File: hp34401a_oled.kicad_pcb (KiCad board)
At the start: 2 copper layers, 30 x 35 mm, 32 parts, among them J1 USB_B_Micro, J2 DISPLAY, J3 UART, J4 FP, J5 DISPLAYPWR, U1 STM32F103C8Tx, U2 LM1117-3.3, Y1 8M

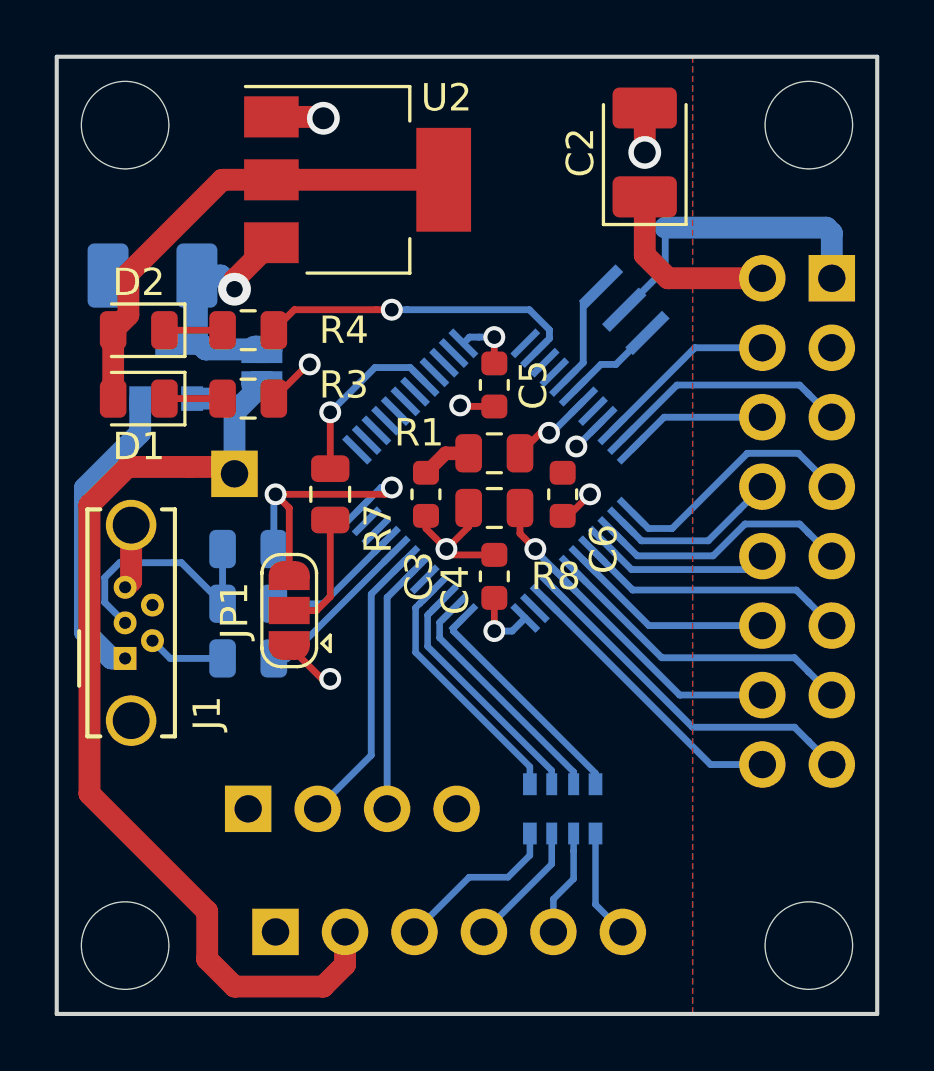
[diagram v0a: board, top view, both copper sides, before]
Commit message: Tweak size, footprints, generate gerber
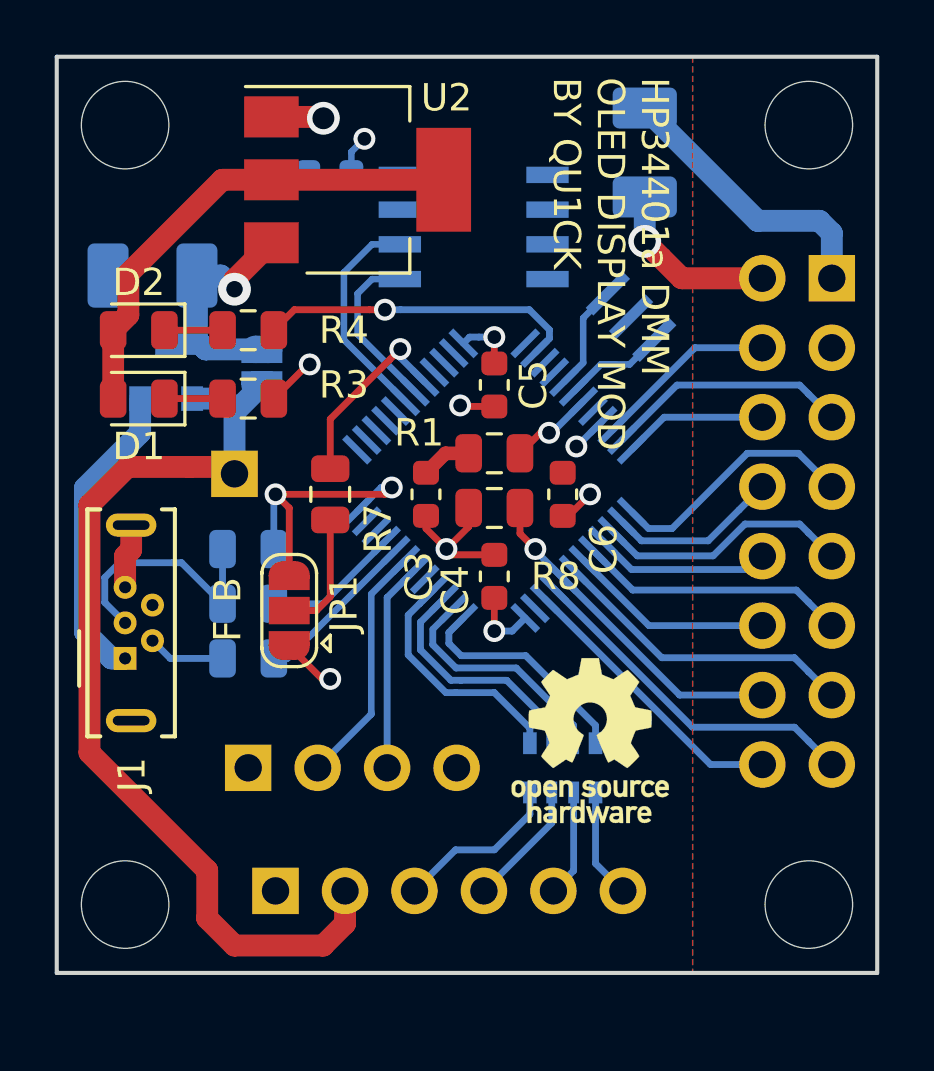
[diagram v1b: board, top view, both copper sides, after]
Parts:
- added C7: 0.1uF, Capacitor_SMD:C_0603_1608Metric, B.Cu at (60.0, 44.3)
- added REF**: OSHW-Logo_5.7x6mm_SilkScreen, Symbol:OSHW-Logo_5.7x6mm_SilkScreen, F.Cu at (69.5, 65.0)
- added U3: AT24C02, Package_SO:SOIC-8_3.9x4.9mm_P1.27mm, B.Cu at (65.2, 46.2)
- C2: moved to B.Cu
- J1: footprint Connector_USB:USB_Micro-B_Wuerth_614105150721_Vertical_CircularHoles -> Connector_USB:USB_Micro-B_Wuerth_614105150721_Vertical
- moved J3 1.50 mm to (57.0, 66.0)
- moved J4 1.50 mm to (58.0, 70.5)
- moved MH3 1.50 mm to (77.5, 71.0)
- moved MH4 1.50 mm to (52.5, 71.0)
- moved RN1 1.50 mm to (68.5, 66.0)
- moved Y1 0.35 mm to (71.0, 49.5)
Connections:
- U1 pad 42: (no net) -> /SCL
- U1 pad 43: (no net) -> /SDA
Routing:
- net /SCL: track 0.00 -> 8.11 mm
- net /SDA: track 0.00 -> 6.22 mm
- net +3V3: track 43.1 -> 46.1 mm, vias 5 -> 7
- net GND: track 29.0 -> 26.3 mm, vias 7 -> 6
- net /USART_TX: track 9.17 -> 7.67 mm
- net /USART_RX: track 10.4 -> 8.93 mm
- net +12V: track 36.5 -> 35.0 mm
- net /BOOT0: track 6.41 -> 7.01 mm
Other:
- board size 30 x 35 mm -> 30 x 33.5 mm
- board text added: "3v3"
- board text added: "B"
- board text added: "F"
- board text added: "GND"
- board text added: "HP34401a DMM OLED DISPLAY MOD BY QU1CK"
- board text added: "INT"
- board text added: "RX"
- board text added: "SCK"
- board text added: "SI"
- board text added: "SO"
- board text added: "TX"
- board text added: "VCC"

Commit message: Few more tweaks
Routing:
- net GND: track 26.3 -> 22.4 mm
- net +3V3: track 46.1 -> 44.0 mm
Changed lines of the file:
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@@
     (thickness 1.6)
     (drawings 21)
-    (tracks 247)
+    (tracks 244)
     (zones 0)
     (modules 35)
@@
   )
   (setup
-    (last_trace_width 0.24)
+    (last_trace_width 0.8)
     (user_trace_width 0.24)
     (user_trace_width 0.25)
@@
     (tags "SMD SMT ceramic resonator filter")
     (attr smd)
-    (fp_text reference Y1 (at 0 2 315) (layer B.SilkS)
+    (fp_text reference Y1 (at 2.828427 1.414214 315) (layer B.SilkS)
       (effects (font (size 1 1) (thickness 0.15)) (justify mirror))
     )
@@
     (tags "capacitor tantalum")
     (attr smd)
-    (fp_text reference C2 (at 0 2.35 90) (layer B.SilkS)
+    (fp_text reference C2 (at 1.5 -2.5 90) (layer B.SilkS)
       (effects (font (size 1 1) (thickness 0.15)) (justify mirror))
     )
@@
   (segment (start 57.85 42.2) (end 59.7 42.2) (width 0.8) (layer F.Cu) (net 1))
   (segment (start 59.7 42.2) (end 59.75 42.25) (width 0.8) (layer F.Cu) (net 1))
-  (segment (start 78.34 46.45) (end 77.89 46) (width 0.8) (layer B.Cu) (net 1))
-  (segment (start 78.34 48.1) (end 78.34 46.45) (width 0.8) (layer B.Cu) (net 1))
-  (segment (start 75.625 46) (end 71.5 41.875) (width 0.8) (layer B.Cu) (net 1))
-  (segment (start 77.89 46) (end 75.625 46) (width 0.8) (layer B.Cu) (net 1))
   (segment (start 52.72 57.125) (end 52.72 58.03) (width 0.8) (layer F.Cu) (net 1))
   (segment (start 52.5 58.25) (end 52.5 59.4) (width 0.8) (layer F.Cu) (net 1))
   (segment (start 52.72 58.03) (end 52.5 58.25) (width 0.8) (layer F.Cu) (net 1))
+  (segment (start 78.34 48.1) (end 76.74 46.5) (width 0.8) (layer B.Cu) (net 1))
+  (segment (start 76.74 46.5) (end 72.5 46.5) (width 0.8) (layer B.Cu) (net 1))
   (segment (start 64.15 44.5) (end 57.85 44.5) (width 0.8) (layer F.Cu) (net 2))
   (segment (start 56.05 44.5) (end 57.85 44.5) (width 0.8) (layer F.Cu) (net 2))
@@
   (segment (start 60.772499 44.255001) (end 60.772499 43.477501) (width 0.24) (layer B.Cu) (net 2))
   (segment (start 60.772499 43.477501) (end 61.25 43) (width 0.24) (layer B.Cu) (net 2))
-  (via blind (at 71.5 46.75) (size 1.2) (drill 0.8) (layers F.Cu B.Cu) (net 2))
-  (segment (start 71.5 45.125) (end 71.5 46.75) (width 0.8) (layer B.Cu) (net 2))
-  (segment (start 75.8 48.1) (end 72.85 48.1) (width 0.8) (layer F.Cu) (net 2))
-  (segment (start 72.85 48.1) (end 72.099999 47.349999) (width 0.8) (layer F.Cu) (net 2))
-  (segment (start 72.099999 47.349999) (end 71.5 46.75) (width 0.8) (layer F.Cu) (net 2))
+  (via (at 73.5 45.25) (size 1.2) (drill 0.8) (layers F.Cu B.Cu) (net 2))
+  (segment (start 71.5 45.125) (end 73.375 45.125) (width 0.8) (layer B.Cu) (net 2))
+  (segment (start 73.375 45.125) (end 73.5 45.25) (width 0.8) (layer B.Cu) (net 2))
+  (segment (start 73.5 48.1) (end 75.8 48.1) (width 0.8) (layer F.Cu) (net 2))
   (segment (start 56.0625 52.5) (end 53.9375 52.5) (width 0.25) (layer F.Cu) (net 3))
   (segment (start 56.0625 50) (end 53.9375 50) (width 0.25) (layer F.Cu) (net 4))
